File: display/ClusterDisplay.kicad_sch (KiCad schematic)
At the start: 67 parts, among them J1 Verdin iMX95, J10 RTC coin cell, J2 Power in, J3 CAN to ECU, J4 Panel LVDS (provisional), J8 JTAG debug, J9 Buttons, Q1 NFET diode, Q2 NFET pass, U1 LM74930-Q1, U2 LM61460-Q1, U3 TLV767-Q1, U4 TCAN1044V-Q1, U5 SN65DSI85-Q1

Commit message: display/: switch to a real bigger round panel, drop the LVDS bridge
Per the user's request to find a slightly larger round display for the
center to maximize the custom faceplate: DisplayModule DM-TFTR50-413
(5.0", 1080x1080, native MIPI-DSI, HX8399 driver, 350 nits, -20 to
60C, $119, real datasheet available) - meaningfully bigger than the
stock 91.44mm speedo opening, and a real, currently-orderable part.

Because this panel speaks MIPI-DSI natively, fascia-pcb's own reason
for the SN65DSI85-Q1 DSI-to-LVDS bridge (its target panel was LVDS-
only, above the Verdin module's native LVDS ceiling) doesn't apply
here - there's no LVDS anywhere in this board's real requirement.
build_panel() replaces build_bridge(): the Verdin's own DSI_1_* pins
now wire straight to a provisional panel connector, no bridge chip, no
VCORE/REFCLK/bypass network. I2C_2_DSI_SDA/SCL (the bridge's own config
bus) are dropped from X1_NETS - real DSI panels configure over the DSI
link itself, not a separate I2C bus. SN65DSI85-Q1 removed from
parts.py/FOOTPRINTS entirely.

kicad-cli sch erc: 5 findings, all real and expected (backlight PWM/
enable + the now-genuinely-unused I2C pins, awaiting the real
DM-TFTR50-413 datasheet; one isolated label awaiting a destination).

Co-Authored-By: Claude Sonnet 5 <noreply@anthropic.com>
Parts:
- removed C14: 1u VCORE, Capacitor_SMD:C_0603_1608Metric, symbol ClusterDisplay:C
- removed C15: 10u 1V8, Capacitor_SMD:C_0603_1608Metric, symbol ClusterDisplay:C
- removed C16, C17, C18, C19, C20, C21: 100n 1V8, Capacitor_SMD:C_0603_1608Metric, symbol ClusterDisplay:C
- removed R22: 10k REFCLK, Resistor_SMD:R_0603_1608Metric, symbol ClusterDisplay:R
- removed U5: SN65DSI85-Q1, Package_QFP:Texas_TQFP-64-1EP_10x10mm_P0.5mm_EP8x8mm_Mask4.44x4.44mm, symbol ClusterDisplay:SN65DSI85-Q1
- J4: value Panel LVDS (provisional) -> Panel MIPI-DSI (provisional); footprint Connector_PinHeader_2.54mm:PinHeader_1x22_P2.54mm_Vertical -> Connector_PinHeader_2.54mm:PinHeader_1x13_P2.54mm_Vertical
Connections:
- net LVDS_A_CLKN is gone; now on net DSI_CLK_N: J4.10 (CLKN)
- net LVDS_A_CLKP is gone; now on net DSI_CLK_P: J4.9 (CLKP)
- net LVDS_A_Y0N is gone; now on net DSI_D0_N: J4.2 (D0N)
- net LVDS_A_Y0P is gone; now on net DSI_D0_P: J4.1 (D0P)
- net LVDS_A_Y1N is gone; now on net DSI_D1_N: J4.4 (D1N)
- net LVDS_A_Y1P is gone; now on net DSI_D1_P: J4.3 (D1P)
- net LVDS_A_Y2N is gone; now on net DSI_D2_N: J4.6 (D2N)
- net LVDS_A_Y2P is gone; now on net DSI_D2_P: J4.5 (D2P)
- net LVDS_A_Y3N is gone; now on net DSI_D3_N: J4.8 (D3N)
- net LVDS_A_Y3P is gone; now on net DSI_D3_P: J4.7 (D3P)
- net LVDS_B_Y0N is gone; now on net GND: J4.12 (GND1)
- net LVDS_B_Y0P is gone; now on net DSI_PANEL_EN: J4.11 (PANEL_EN)
- net LVDS_B_Y1P is gone; now on net GND: J4.13 (GND2)
- net GND: no longer J4.21 (GND1), J4.22 (GND2)
- net DSI_BRIDGE_EN renamed DSI_PANEL_EN
- net DSI_I2C_SCL: no longer names the net of J1.55 (I2C_2_DSI_SCL)
- net DSI_I2C_SDA: no longer names the net of J1.53 (I2C_2_DSI_SDA)
- removed net LVDS_B_CLKN: J4.20 (B_CLKN)
- removed net LVDS_B_CLKP: J4.19 (B_CLKP)
- removed net LVDS_B_Y1N: J4.14 (B_Y1N)
- removed net LVDS_B_Y2N: J4.16 (B_Y2N)
- removed net LVDS_B_Y2P: J4.15 (B_Y2P)
- removed net LVDS_B_Y3N: J4.18 (B_Y3N)
- removed net LVDS_B_Y3P: J4.17 (B_Y3P)
- no-connect marks 197 -> 185

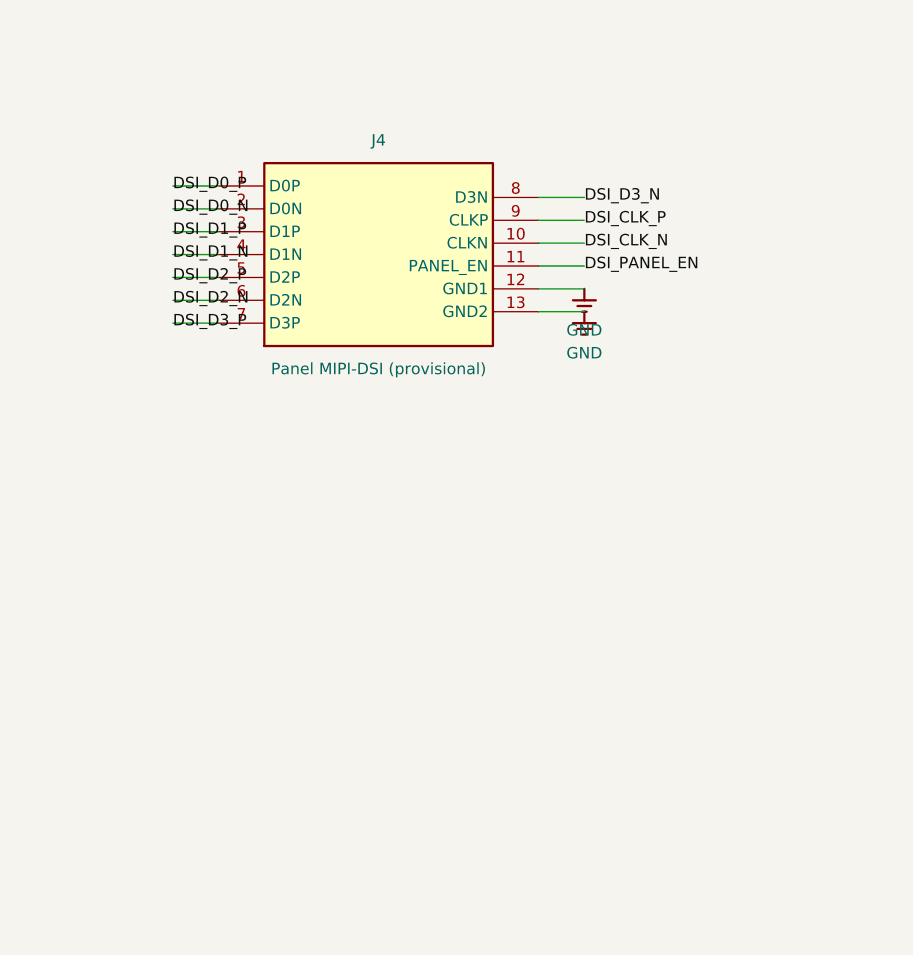
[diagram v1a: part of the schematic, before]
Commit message: Wire the real DM-TFTR50-413 connector; surface two new real requirements
Pulled DisplayModule's actual DM-TFTR50-413 datasheet PDF and read the
full 50-pin FPC pinout (section 3.1) and mechanical drawing (4.1).

CONN_PANEL is now a real part, not provisional: the mechanical drawing
specifies "CONNECTOR: JF40C-50DP-0.4V(51), Hirose" - an OCR mangle of
Hirose DF40C-50DP-0.4V(51), confirmed real/stocked and matched exactly
against KiCad's own bundled footprint
(Connector_Hirose_DF40:Hirose_DF40C-50DP-0.4V_2x25-1MP_P0.4mm, 2x25 =
50 positions). All 50 real pins wired per the datasheet's own table:
4 DSI lanes + clock to the existing X1 nets, GND, IOVCC->+1V8, VSP-
>+5V (both real fits with the existing rails), RESET->the panel-enable
net, and ID_PIN1/ID_PIN2/LEDPWM/TE explicitly NoConnect per the
datasheet's own "if not used, open" guidance.

The real pinout also surfaced two genuine new circuit requirements
this board didn't have before, left as real named label stubs rather
than guessed at:
  - VSN (pins 30/32): a real -5V analog rail the panel's TFT gate
    drive needs. No source for it yet - needs a real inverting
    regulator/charge pump, part TBD.
  - LEDA/LEDK (backlight): NOT a simple low-voltage LED like the aux
    gauges use. Datasheet section 5.4: 6 white LEDs in series
    internally, VF=37.2V typ (38.4V max) - needs a real ~38V boost LED
    driver, not a series resistor. Part TBD.

kicad-cli sch erc: 6 findings, all real and expected - VSN correctly
flagged power_pin_not_driven (that circuit genuinely doesn't exist
yet), same baseline items as before otherwise.

Co-Authored-By: Claude Sonnet 5 <noreply@anthropic.com>
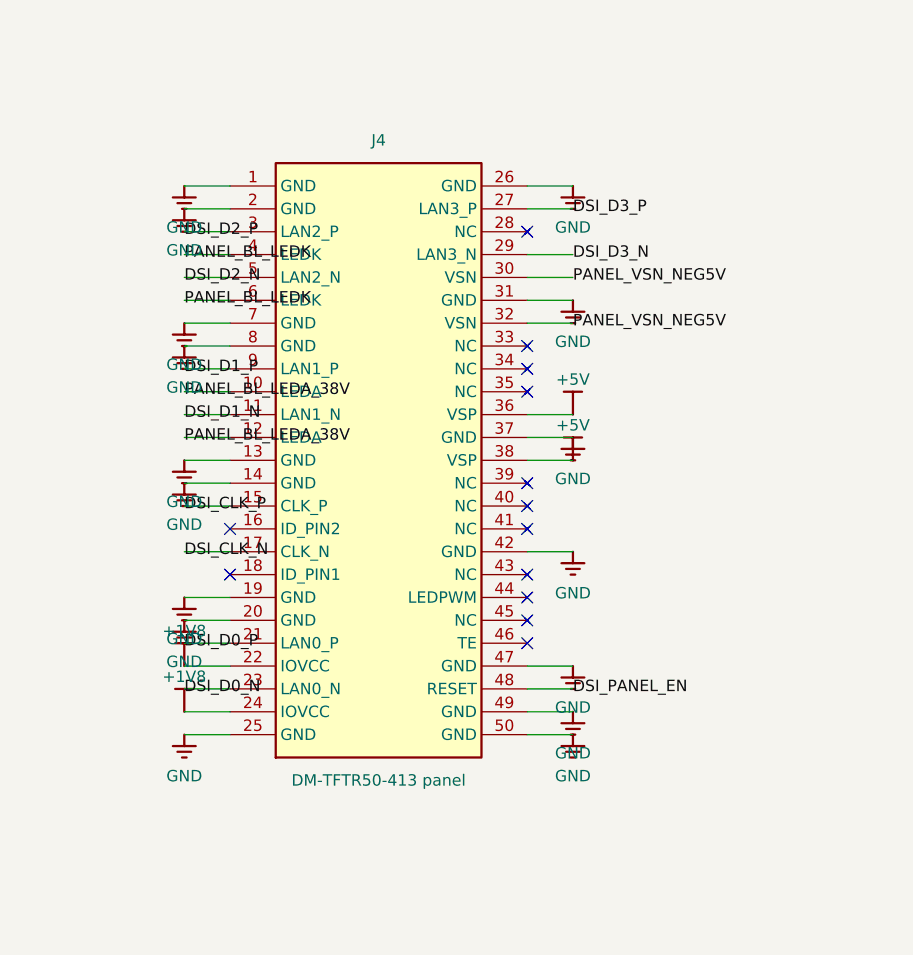
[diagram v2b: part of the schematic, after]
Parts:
- J4: value Panel MIPI-DSI (provisional) -> DM-TFTR50-413 panel; footprint Connector_PinHeader_2.54mm:PinHeader_1x13_P2.54mm_Vertical -> Connector_Hirose_DF40:Hirose_DF40C-50DP-0.4V_2x25-1MP_P0.4mm
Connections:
- net +1V8: now also J4.22 (IOVCC), J4.24 (IOVCC)
- net +5V: now also J4.36 (VSP), J4.38 (VSP)
- net DSI_CLK_N: now also J4.17 (CLK_N); no longer J4.10 (CLKN)
- net DSI_CLK_P: now also J4.15 (CLK_P); no longer J4.9 (CLKP)
- net DSI_D0_N: now also J4.23 (LAN0_N); no longer J4.2 (D0N)
- net DSI_D0_P: now also J4.21 (LAN0_P); no longer J4.1 (D0P)
- net DSI_D1_N: now also J4.11 (LAN1_N); no longer J4.4 (D1N)
- net DSI_D1_P: now also J4.9 (LAN1_P); no longer J4.3 (D1P)
- net DSI_D2_N: now also J4.5 (LAN2_N); no longer J4.6 (D2N)
- net DSI_D2_P: now also J4.3 (LAN2_P); no longer J4.5 (D2P)
- net DSI_D3_N: now also J4.29 (LAN3_N); no longer J4.8 (D3N)
- net DSI_D3_P: now also J4.27 (LAN3_P); no longer J4.7 (D3P)
- net DSI_PANEL_EN: now also J4.48 (RESET); no longer J4.11 (PANEL_EN)
- net GND: now also J4.1 (GND), J4.14 (GND), J4.19 (GND), J4.2 (GND), J4.20 (GND), J4.25 (GND), J4.26 (GND), J4.31 (GND), J4.37 (GND), J4.42 (GND), J4.47 (GND), J4.49 (GND), J4.50 (GND), J4.7 (GND), J4.8 (GND); no longer J4.12 (GND1)
- new net PANEL_BL_LEDA_38V: J4.10 (LEDA), J4.12 (LEDA)
- new net PANEL_BL_LEDK: J4.4 (LEDK), J4.6 (LEDK)
- new net PANEL_VSN_NEG5V: J4.30 (VSN), J4.32 (VSN)
- no-connect marks 185 -> 198

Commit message: Design the two real circuits the DM-TFTR50-413 pinout surfaced
Real parts research for the -5V rail and backlight boost driver flagged
last commit, now designed and wired:

VSN (-5V panel gate-drive rail): TI TPS60403-Q1, AEC-Q100 Grade 1,
5-pin SOT-23 charge-pump inverter - its own datasheet lists "Automotive
Cluster" and "LCD Displays" as named applications. Real 3-cap circuit
straight from the datasheet's own typical application (1uF Cfly/CI/CO),
IN on +5V (not +12V_PROT - the part's absolute max input is 5.25V).

Backlight (6 series white LEDs, VF 37.2V typ/38.4V max, IF 20mA):
Diodes Inc AL8853AQ, AEC-Q100 Grade 1, SO-8 automotive boost LED
controller - lists "Infotainment and cluster backlight displays" as a
named application. Full real component sizing from the panel's own
datasheet numbers and AL8853AQ's own design equations: R_FB=10.0R sets
20mA LED current, L1=680uH sized for 0.4 ripple ratio at nominal 12V,
R_CS=2.00R sets OCP 30% above the real worst-case peak current at 9V
(automotive low-line), R4/R5=232k/10.0k sets the OVP threshold to 48V
(25% margin over the panel's own 38.4V max). VIN on +12V_PROT (AL8853AQ's
6V minimum is above the 5V rail). Q3 (boost switch) and D2 (rectifier)
reuse this file's existing generic NFET/TVS symbols with real voltage/
current requirements cited - exact automotive part numbers still TBD,
same "right footprint, real part pending" status CONN_PANEL had before
its own datasheet pull. PWM tied to +5V for an always-on baseline;
real Verdin-driven dimming is a flagged future enhancement.

kicad-cli sch erc: 5 findings, down from 6 - VSN's power_pin_not_driven
is gone, resolved by the real circuit. No new findings introduced.

Co-Authored-By: Claude Sonnet 5 <noreply@anthropic.com>
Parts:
- removed L1: 2.2u, Inductor_SMD:L_1210_3225Metric, symbol ClusterDisplay:L
- added C40: 1u Cfly (AEC-Q200), Capacitor_SMD:C_0603_1608Metric, symbol ClusterDisplay:C
- added C41: 1u CI (AEC-Q200), Capacitor_SMD:C_0603_1608Metric, symbol ClusterDisplay:C
- added C42: 1u CO (AEC-Q200), Capacitor_SMD:C_0603_1608Metric, symbol ClusterDisplay:C
- added C43: 1u VIN (AEC-Q200), Capacitor_SMD:C_0603_1608Metric, symbol ClusterDisplay:C
- added C44: 10n COMP (typical, not loop-verified), Capacitor_SMD:C_0603_1608Metric, symbol ClusterDisplay:C
- added C45: 1u VOUT, 63V-rated (AEC-Q200), Capacitor_SMD:C_0603_1608Metric, symbol ClusterDisplay:C
- added D2: Schottky rectifier (VRRM >=58V, IF>=60mA, part TB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, Diode_SMD:D_SMB, symbol ClusterDisplay:TVS
- added L1: 680u boost inductor (real, see docstring math), Inductor_SMD:L_1210_3225Metric, symbol ClusterDisplay:L
- added L1: 2.2u, Inductor_SMD:L_1210_3225Metric, symbol ClusterDisplay:L
- added Q3: NFET boost switch (BVDSS >=58V, part TBD), Package_TO_SOT_SMD:SOT-23, symbol ClusterDisplay:NFET
- added R37: 2.00R OCP/CS sense (real, see docstring math), Resistor_SMD:R_0603_1608Metric, symbol ClusterDisplay:R
- added R38: 232k OVP top (real, see docstring math), Resistor_SMD:R_0603_1608Metric, symbol ClusterDisplay:R
- added R39: 10.0k OVP bottom (real, see docstring math), Resistor_SMD:R_0603_1608Metric, symbol ClusterDisplay:R
- added R40: 10.0R LED FB (real, see docstring math), Resistor_SMD:R_0603_1608Metric, symbol ClusterDisplay:R
- added U6: TPS60403-Q1, Package_TO_SOT_SMD:SOT-23-5, symbol ClusterDisplay:TPS60403-Q1
- added U7: AL8853AQ, Package_SO:SOIC-8_3.9x4.9mm_P1.27mm, symbol ClusterDisplay:AL8853AQ
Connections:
- net +12V_PROT: now also C43.1, L1.1, U7.1 (VIN)
- net +5V: now also C41.1, L1.2, U6.2 (IN), U7.8 (PWM)
- net GND: now also C41.2, C42.2, C43.2, C44.2, C45.2, R37.2, R39.2, R40.2, U6.4 (GND), U7.3 (GND)
- net PANEL_BL_LEDA_38V: now also C45.1, D2.2, R38.1
- net PANEL_BL_LEDK: now also R40.1, U7.5 (FB)
- net PANEL_VSN_NEG5V: now also C42.1, U6.1 (OUT)
- net SW_5V: now also L1.1
- new net BL_COMP: C44.1, U7.6 (COMP)
- new net BL_CS_NODE: Q3.3 (S), R37.1, U7.4 (CS)
- new net BL_GATE: Q3.1 (G), U7.2 (GATE)
- new net BL_OVP_DIV: R38.2, R39.1, U7.7 (OVP)
- new net BL_SW: D2.1, L1.2, Q3.2 (D)
- new net VSN_CFLY_N: C40.2, U6.3 (CFLYN)
- new net VSN_CFLY_P: C40.1, U6.5 (CFLYP)

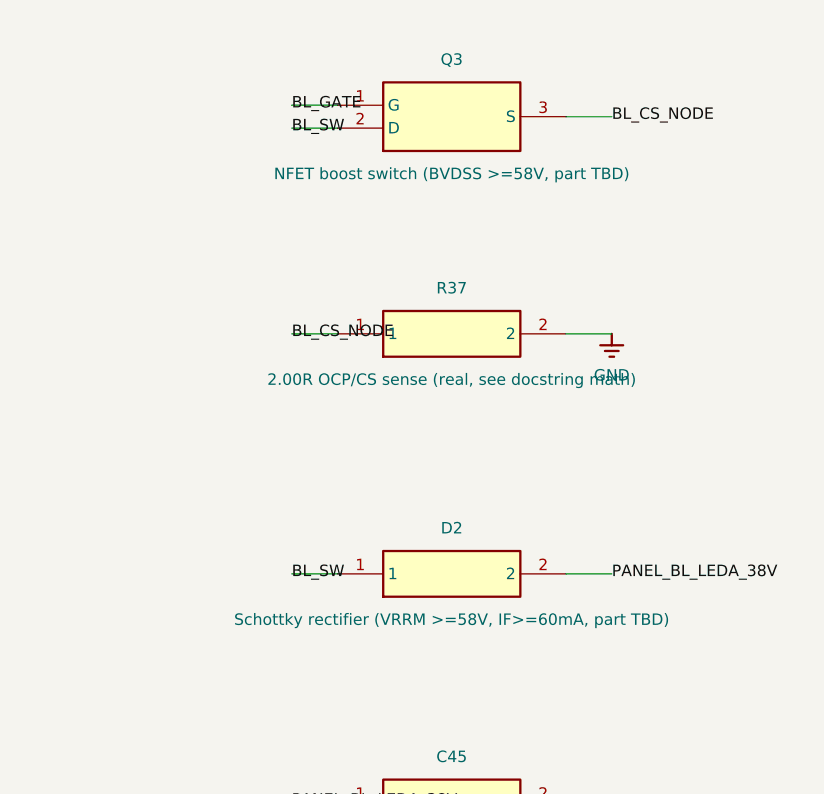
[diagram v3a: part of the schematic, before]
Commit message: Name the boost FET and Schottky diode: real automotive parts
Closes out the backlight driver design started last commit. Both
found and verified against real distributor/manufacturer listings:

Q3 (boost switch): Meritek MFT6N2A5S23A - AEC-Q101, SOT-23, 60V/2.5A,
RDS(on)=75mOhm max. Real margin over both requirements (BVDSS vs the
48V OVP threshold; current rating vs the real ~113mA peak this circuit
ever sees).

D2 (rectifier): Nexperia PMEG6010ELRX - AEC-Q101, SOD-123W, 60V VRRM,
1A average forward current. Needed its own dedicated symbol
(SCHOTTKY_SOD123W) rather than reusing the shared TVS symbol - the
real part's package (SOD-123W) differs from the TVS clamp diodes'
D_SMB footprint used elsewhere on this board. Footprint confirmed
against KiCad's own bundled library (Diode_SMD:Nexperia_CFP3_SOD-123W).

kicad-cli sch erc: same 5 documented findings, no new issues.

Co-Authored-By: Claude Sonnet 5 <noreply@anthropic.com>
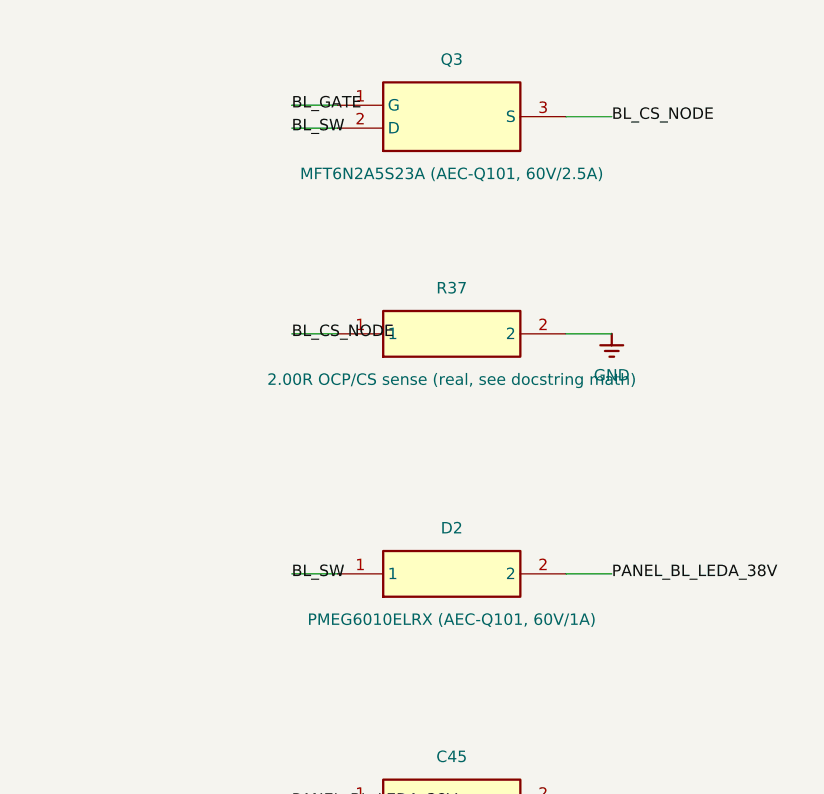
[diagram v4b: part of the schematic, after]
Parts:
- removed D2: Schottky rectifier (VRRM >=58V, IF>=60mA, part TB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, Diode_SMD:D_SMB, symbol ClusterDisplay:TVS
- removed L1: 680u boost inductor (real, see docstring math), Inductor_SMD:L_1210_3225Metric, symbol ClusterDisplay:L
- removed L1: 2.2u, Inductor_SMD:L_1210_3225Metric, symbol ClusterDisplay:L
- added D2: PMEG6010ELRX (AEC-Q101, 60V/1A), Diode_SMD:Nexperia_CFP3_SOD-123W, symbol ClusterDisplay:SCHOTTKY_SOD123W
- added L1: 2.2u, Inductor_SMD:L_1210_3225Metric, symbol ClusterDisplay:L
- added L1: 680u boost inductor (real, see docstring math), Inductor_SMD:L_1210_3225Metric, symbol ClusterDisplay:L
- Q3: value NFET boost switch (BVDSS >=58V, part TBD) -> MFT6N2A5S23A (AEC-Q101, 60V/2.5A)
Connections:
- net +12V_PROT: now also L1.1
- net +5V: now also L1.2
- net BL_SW: now also D2.1, L1.2
- net PANEL_BL_LEDA_38V: now also D2.2
- net SW_5V: now also L1.1

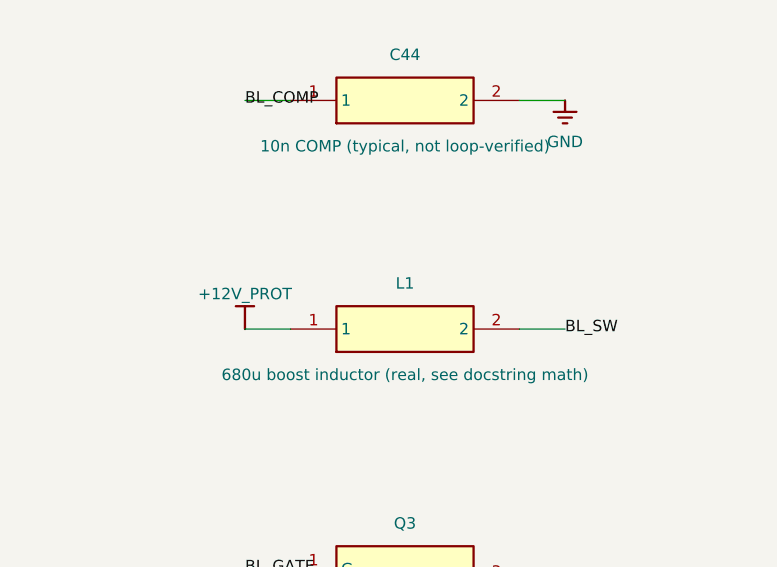
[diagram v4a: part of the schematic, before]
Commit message: Fix a real duplicate reference: backlight inductor was L1, same as the power tree's own buck inductor
Caught while preparing for PCB layout, not by ERC (KiCad's own ERC
doesn't flag duplicate references the way it flags electrical issues).
Real consequence if this had reached build_pcb.py: that script reads
parts back out of the schematic keyed by reference string, so the
second "L1" instance would have silently overwritten the first in the
parts dict - one of the two real inductors would have vanished from
the board with no error, not even a net-count mismatch (since both
inductors' own net names differ, the assertion checking sch-vs-PCB net
pin counts per net wouldn't have caught a whole missing footprint).

Renamed the backlight boost inductor to L2.

Co-Authored-By: Claude Sonnet 5 <noreply@anthropic.com>
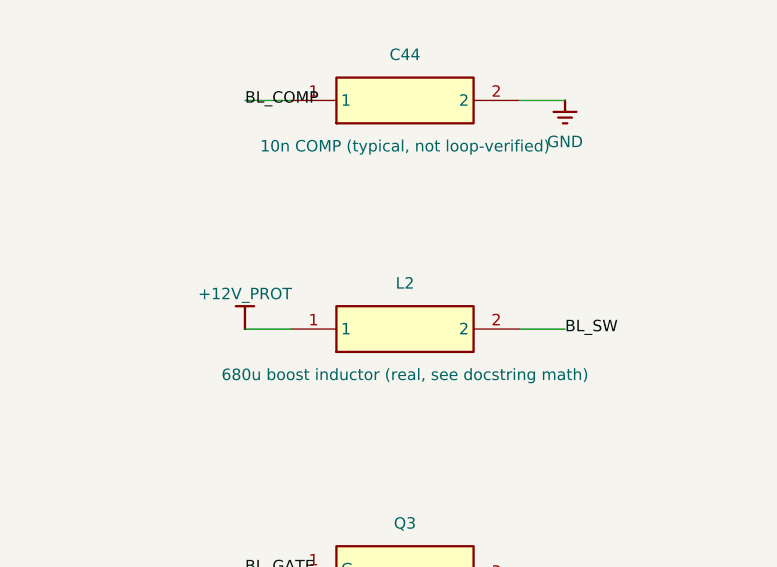
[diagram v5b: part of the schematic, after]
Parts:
- removed L1: 2.2u, Inductor_SMD:L_1210_3225Metric, symbol ClusterDisplay:L
- removed L1: 680u boost inductor (real, see docstring math), Inductor_SMD:L_1210_3225Metric, symbol ClusterDisplay:L
- added L1: 2.2u, Inductor_SMD:L_1210_3225Metric, symbol ClusterDisplay:L
- added L2: 680u boost inductor (real, see docstring math), Inductor_SMD:L_1210_3225Metric, symbol ClusterDisplay:L
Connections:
- net +12V_PROT: now also L2.1
- net +5V: now also L1.2
- net BL_SW: now also L2.2
- net SW_5V: now also L1.1
